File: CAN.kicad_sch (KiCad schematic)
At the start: 5 parts

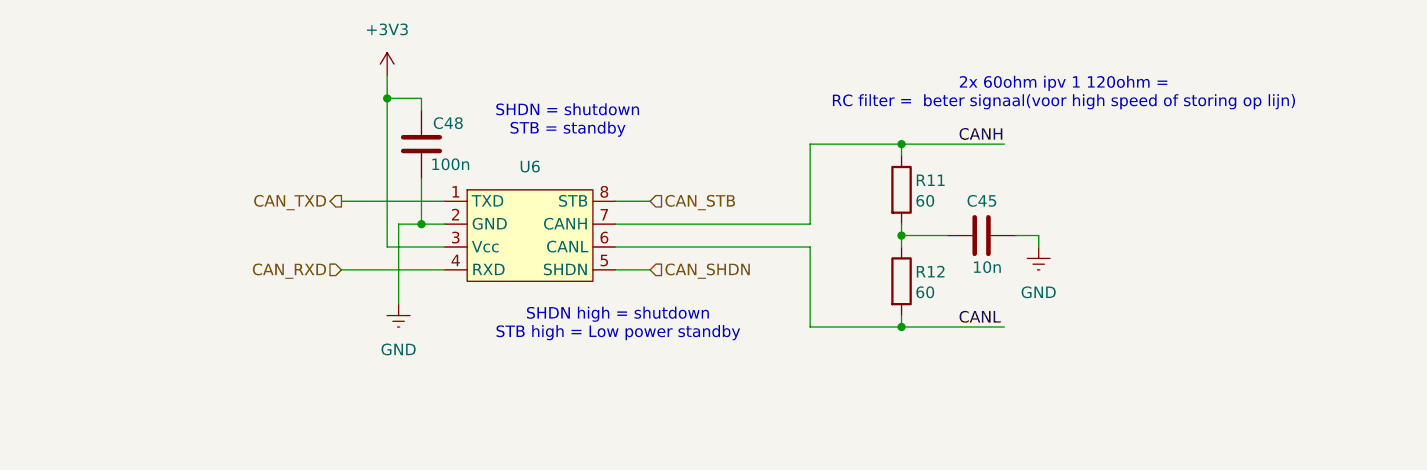
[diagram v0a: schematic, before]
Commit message: footprints
footprints aan de condensators toegevoegd
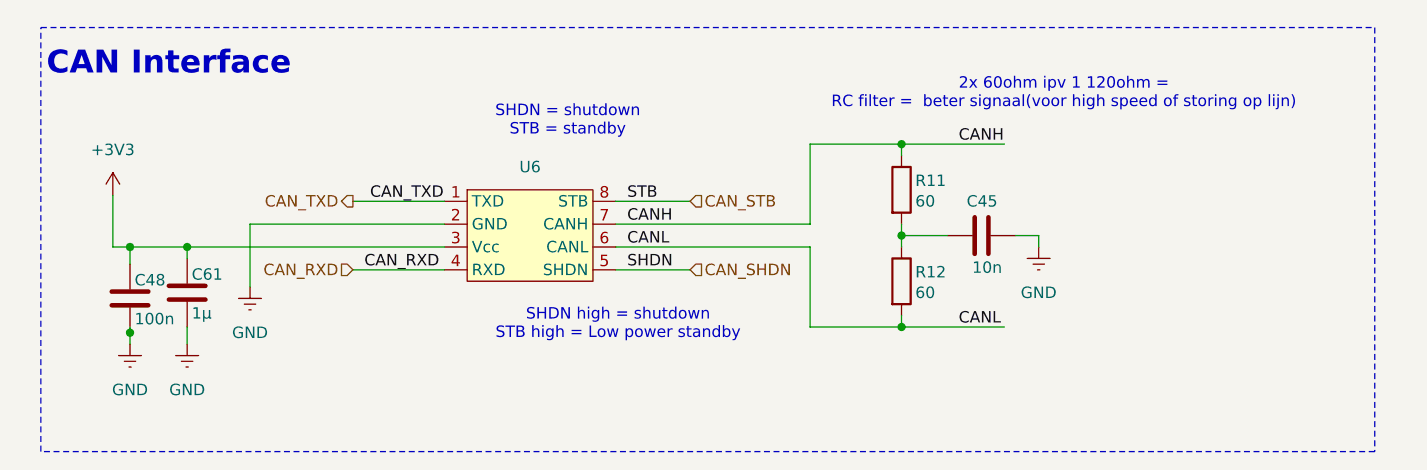
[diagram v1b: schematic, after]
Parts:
- added C61: 1µ, Capacitor_SMD:C_0603_1608Metric, symbol Device:C
- C48: footprint EEPROM:579-24LC32AFT-ISN -> Capacitor_SMD:C_0603_1608Metric
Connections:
- net +3V3: now also C61.1
- net GND: now also C61.2
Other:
- note added: "CAN Interface"

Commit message: schemas klaar
schemas en footprints aan symbolen allemaal juist gemaakt
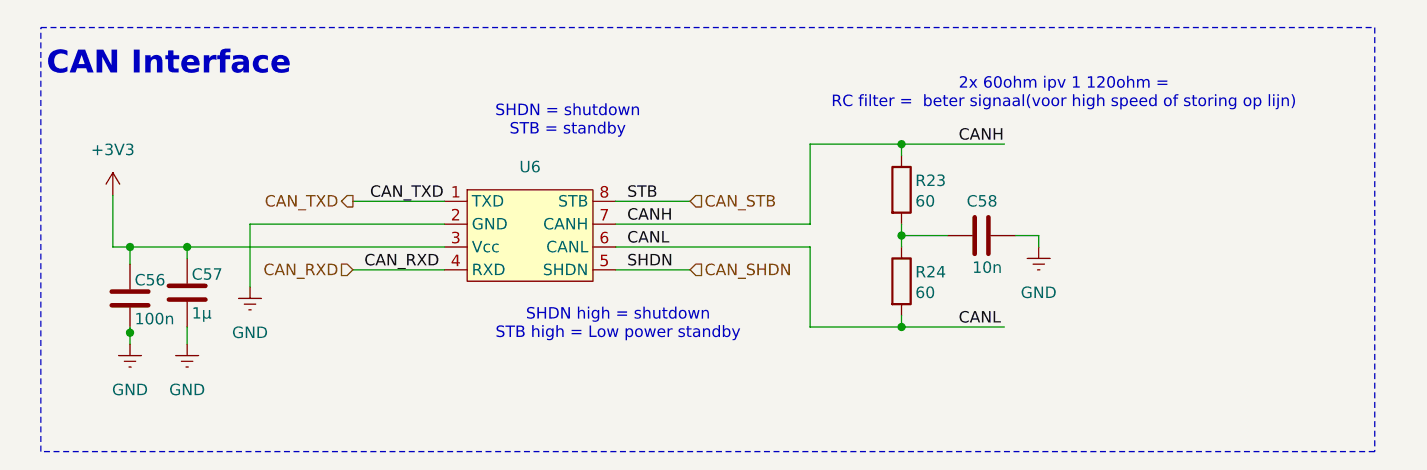
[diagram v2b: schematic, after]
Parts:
- C58: renamed from C45; footprint EEPROM:579-24LC32AFT-ISN -> Capacitor_SMD:C_0603_1608Metric
- R23: renamed from R11; footprint (none) -> Resistor_SMD:R_0603_1608Metric
- R24: renamed from R12; footprint (none) -> Resistor_SMD:R_0603_1608Metric
- renumbered C48 to C56, C61 to C57
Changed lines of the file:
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@@
 		(dnp no)
 		(fields_autoplaced yes)
-		(property "Reference" "#PWR070"
+		(property "Reference" "#PWR069"
 			(at 95.885 97.155 0)
 			(hide yes)
@@
 			(project "ESC_PLC"
 				(path "/5bd3bb6f-fe53-443c-806c-077e2bbb5d14/fe40b710-6ad0-4f5f-80cc-5572b327525f"
-					(reference "#PWR070")
+					(reference "#PWR069")
 					(unit 1)
 				)
@@
 		(in_pos_files yes)
 		(dnp no)
-		(property "Reference" "C61"
+		(property "Reference" "C57"
 			(at 96.393 83.058 0)
 			(show_name no)
@@
 			(project "ESC_PLC"
 				(path "/5bd3bb6f-fe53-443c-806c-077e2bbb5d14/fe40b710-6ad0-4f5f-80cc-5572b327525f"
-					(reference "C61")
+					(reference "C57")
 					(unit 1)
 				)
@@
 		(dnp no)
 		(fields_autoplaced yes)
-		(property "Reference" "#PWR071"
+		(property "Reference" "#PWR068"
 			(at 89.535 97.155 0)
 			(hide yes)
@@
 			(project "ESC_PLC"
 				(path "/5bd3bb6f-fe53-443c-806c-077e2bbb5d14/fe40b710-6ad0-4f5f-80cc-5572b327525f"
-					(reference "#PWR071")
+					(reference "#PWR068")
 					(unit 1)
 				)
@@
 		(dnp no)
 		(fields_autoplaced yes)
-		(property "Reference" "#PWR047"
+		(property "Reference" "#PWR070"
 			(at 102.87 90.805 0)
 			(hide yes)
@@
 			(project "ESC_PLC"
 				(path "/5bd3bb6f-fe53-443c-806c-077e2bbb5d14/fe40b710-6ad0-4f5f-80cc-5572b327525f"
-					(reference "#PWR047")
+					(reference "#PWR070")
 					(unit 1)
 				)
@@
 		(in_pos_files yes)
 		(dnp no)
-		(property "Reference" "R12"
+		(property "Reference" "R24"
 			(at 176.784 82.804 0)
 			(show_name no)
@@
 			)
 		)
-		(property "Footprint" ""
+		(property "Footprint" "Resistor_SMD:R_0603_1608Metric"
 			(at 173.482 83.82 90)
 			(hide yes)
@@
 			(project "ESC_PLC"
 				(path "/5bd3bb6f-fe53-443c-806c-077e2bbb5d14/fe40b710-6ad0-4f5f-80cc-5572b327525f"
-					(reference "R12")
+					(reference "R24")
 					(unit 1)
 				)
@@
 		(dnp no)
 		(fields_autoplaced yes)
-		(property "Reference" "#PWR049"
+		(property "Reference" "#PWR071"
 			(at 190.5 86.36 0)
 			(hide yes)
@@
 			(project "ESC_PLC"
 				(path "/5bd3bb6f-fe53-443c-806c-077e2bbb5d14/fe40b710-6ad0-4f5f-80cc-5572b327525f"
-					(reference "#PWR049")
+					(reference "#PWR071")
 					(unit 1)
 				)
@@
 		(dnp no)
 		(fields_autoplaced yes)
-		(property "Reference" "#PWR048"
+		(property "Reference" "#PWR067"
 			(at 87.63 78.105 0)
 			(hide yes)
@@
 			(project "ESC_PLC"
 				(path "/5bd3bb6f-fe53-443c-806c-077e2bbb5d14/fe40b710-6ad0-4f5f-80cc-5572b327525f"
-					(reference "#PWR048")
+					(reference "#PWR067")
 					(unit 1)
 				)
@@
 		(in_pos_files yes)
 		(dnp no)
-		(property "Reference" "C48"
+		(property "Reference" "C56"
 			(at 90.043 83.693 0)
 			(show_name no)
@@
 			(project "ESC_PLC"
 				(path "/5bd3bb6f-fe53-443c-806c-077e2bbb5d14/fe40b710-6ad0-4f5f-80cc-5572b327525f"
-					(reference "C48")
+					(reference "C56")
 					(unit 1)
 				)
@@
 		(in_pos_files yes)
 		(dnp no)
-		(property "Reference" "C45"
+		(property "Reference" "C58"
 			(at 185.928 74.93 90)
 			(show_name no)
@@
 			)
 		)
-		(property "Footprint" "EEPROM:579-24LC32AFT-ISN"
+		(property "Footprint" "Capacitor_SMD:C_0603_1608Metric"
 			(at 187.96 77.7748 0)
 			(hide yes)
@@
 			(project "ESC_PLC"
 				(path "/5bd3bb6f-fe53-443c-806c-077e2bbb5d14/fe40b710-6ad0-4f5f-80cc-5572b327525f"
-					(reference "C45")
+					(reference "C58")
 					(unit 1)
 				)
@@
 		(in_pos_files yes)
 		(dnp no)
-		(property "Reference" "R11"
+		(property "Reference" "R23"
 			(at 176.784 72.644 0)
 			(show_name no)
@@
 			)
 		)
-		(property "Footprint" ""
+		(property "Footprint" "Resistor_SMD:R_0603_1608Metric"
 			(at 173.482 73.66 90)
 			(hide yes)
@@
 			(project "ESC_PLC"
 				(path "/5bd3bb6f-fe53-443c-806c-077e2bbb5d14/fe40b710-6ad0-4f5f-80cc-5572b327525f"
-					(reference "R11")
-					(unit 1)
-				)
+					(reference "R23")
+					(unit 1)
+				)

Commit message: al de main blokken bij elkaar gezet op juiste plaats
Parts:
- added D5: NUP2105L, Package_TO_SOT_SMD:SOT-23, symbol Power_Protection:NUP2105L
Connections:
- net CANH: now also D5.1 (K)
- net CANL: now also D5.2 (K)
- net GND: now also D5.3 (A)
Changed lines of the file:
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@@
+	)
+	(junction
+		(at 205.74 88.9)
+		(diameter 0)
+		(color 0 0 0 0)
 	)
 	(junction
@@
 	)
 	(junction
+		(at 196.85 68.58)
+		(diameter 0)
+		(color 0 0 0 0)
+	)
+	(junction
 		(at 89.535 89.535)
 		(diameter 0)
@@
 	(wire
 		(pts
+			(xy 199.39 81.28) (xy 199.39 82.55)
+		)
+		(stroke
+			(width 0)
+			(type default)
+		)
+	)
+	(wire
+		(pts
 			(xy 87.63 80.01) (xy 89.535 80.01)
 		)
@@
 	(wire
 		(pts
+			(xy 201.93 69.85) (xy 201.93 71.12)
+		)
+		(stroke
+			(width 0)
+			(type default)
+		)
+	)
+	(wire
+		(pts
 			(xy 89.535 89.535) (xy 89.535 90.805)
 		)
@@
 	(wire
 		(pts
+			(xy 196.85 68.58) (xy 209.55 68.58)
+		)
+		(stroke
+			(width 0)
+			(type default)
+		)
+	)
+	(wire
+		(pts
 			(xy 175.26 78.74) (xy 180.34 78.74)
 		)
@@
 	(wire
 		(pts
+			(xy 205.74 69.85) (xy 205.74 88.9)
+		)
+		(stroke
+			(width 0)
+			(type default)
+		)
+	)
+	(wire
+		(pts
+			(xy 205.74 88.9) (xy 209.55 88.9)
+		)
+		(stroke
+			(width 0)
+			(type default)
+		)
+	)
+	(wire
+		(pts
+			(xy 196.85 68.58) (xy 196.85 71.12)
+		)
+		(stroke
+			(width 0)
+			(type default)
+		)
+	)
+	(wire
+		(pts
+			(xy 201.93 69.85) (xy 205.74 69.85)
+		)
+		(stroke
+			(width 0)
+			(type default)
+		)
+	)
+	(wire
+		(pts
 			(xy 95.885 88.9) (xy 95.885 90.805)
 		)
@@
 	(wire
 		(pts
-			(xy 175.26 68.58) (xy 186.69 68.58)
+			(xy 175.26 68.58) (xy 196.85 68.58)
 		)
 		(stroke
@@
 	(wire
 		(pts
-			(xy 175.26 88.9) (xy 186.69 88.9)
+			(xy 175.26 88.9) (xy 205.74 88.9)
 		)
 		(stroke
@@
 	)
 	(label "CANH"
-		(at 181.61 68.58 0)
+		(at 209.55 68.58 0)
 		(effects
 			(font
@@
 	)
 	(label "CANL"
-		(at 181.61 88.9 0)
+		(at 209.55 88.9 0)
 		(effects
 			(font
@@
 	)
 	(symbol
+		(lib_id "Power_Protection:NUP2105L")
+		(at 199.39 76.2 0)
+		(unit 1)
+		(body_style 1)
+		(exclude_from_sim no)
+		(in_bom yes)
+		(on_board yes)
+		(in_pos_files yes)
+		(dnp no)
+		(property "Reference" "D5"
+			(at 206.502 74.168 0)
+			(show_name no)
+			(do_not_autoplace no)
+			(effects
+				(font
+					(size 1.27 1.27)
+				)
+				(justify left)
+			)
+		)
+		(property "Value" "NUP2105L"
+			(at 206.756 76.454 0)
+			(show_name no)
+			(do_not_autoplace no)
+			(effects
+				(font
+					(size 1.27 1.27)
+				)
+				(justify left)
+			)
+		)
+		(property "Footprint" "Package_TO_SOT_SMD:SOT-23"
+			(at 205.105 77.47 0)
+			(hide yes)
+			(show_name no)
+			(do_not_autoplace no)
+			(effects
+				(font
+					(size 1.27 1.27)
+				)
+				(justify left)
+			)
+		)
+		(property "Datasheet" "https://www.onsemi.com/pub_link/Collateral/NUP2105L-D.PDF"
+			(at 202.565 73.025 0)
+			(hide yes)
+			(show_name no)
+			(do_not_autoplace no)
+			(effects
+				(font
+					(size 1.27 1.27)
+				)
+			)
+		)
+		(property "Description" "Dual Line CAN Bus Protector, 24Vrwm"
+			(at 199.39 76.2 0)
+			(hide yes)
+			(show_name no)
+			(do_not_autoplace no)
+			(effects
+				(font
+					(size 1.27 1.27)
+				)
+			)
+		)
+		(pin "1"
+		)
+		(pin "3"
+		)
+		(pin "2"
+		)
+		(instances
+			(project "ESC_PLC"
+				(path "/5bd3bb6f-fe53-443c-806c-077e2bbb5d14/fe40b710-6ad0-4f5f-80cc-5572b327525f"
+					(reference "D5")
+					(unit 1)
+				)
+			)
+		)
+	)
+	(symbol
 		(lib_id "power:GNDREF")
 		(at 102.87 84.455 0)
@@
 		(in_pos_files yes)
 		(dnp no)
-		(fields_autoplaced yes)
 		(property "Reference" "#PWR071"
 			(at 190.5 86.36 0)
@@
 		)
 		(property "Value" "GND"
-			(at 190.5 85.09 0)
+			(at 190.5 84.328 0)
 			(show_name no)
 			(do_not_autoplace no)
@@
 					(unit 1)
 				)
+			)
+		)
+	)
+	(symbol
+		(lib_id "power:GNDREF")
+		(at 199.39 82.55 0)
+		(unit 1)
+		(body_style 1)
+		(exclude_from_sim no)
+		(in_bom yes)
+		(on_board yes)
+		(in_pos_files yes)
+		(dnp no)
+		(property "Reference" "#PWR0105"
+			(at 199.39 88.9 0)
+			(hide yes)
+			(show_name no)
+			(do_not_autoplace no)
+			(effects
+				(font
+					(size 1.27 1.27)
+				)
+			)
+		)
+		(property "Value" "GND"
+			(at 199.39 86.614 0)
+			(show_name no)
+			(do_not_autoplace no)
+			(effects
+				(font
+					(size 1.27 1.27)
+				)
+			)
+		)
+		(property "Footprint" ""
+			(at 199.39 82.55 0)
+			(hide yes)
+			(show_name no)
+			(do_not_autoplace no)
+			(effects
+				(font
+					(size 1.27 1.27)
+				)
+			)
+		)
+		(property "Datasheet" ""
+			(at 199.39 82.55 0)
+			(hide yes)
+			(show_name no)
+			(do_not_autoplace no)
+			(effects
+				(font
+					(size 1.27 1.27)
+				)
+			)
+		)
+		(property "Description" "Power symbol creates a global label with name \"GNDREF\" , reference supply ground"
+			(at 199.39 82.55 0)
+			(hide yes)
+			(show_name no)
+			(do_not_autoplace no)
+			(effects
+				(font
+					(size 1.27 1.27)
+				)
+			)
+		)
+		(pin "1"
+		)
+		(instances
+			(project "ESC_PLC"
+				(path "/5bd3bb6f-fe53-443c-806c-077e2bbb5d14/fe40b710-6ad0-4f5f-80cc-5572b327525f"
+					(reference "#PWR0105")
+					(unit 1)
+				)

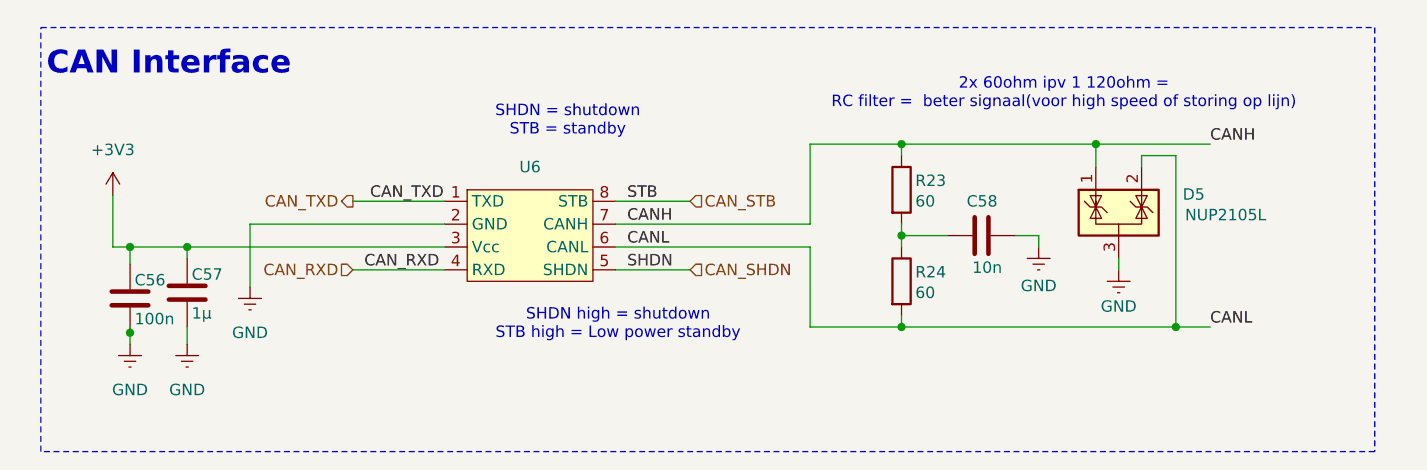
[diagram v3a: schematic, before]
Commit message: connector
connector toegevoegd en wat pinnen aangepast
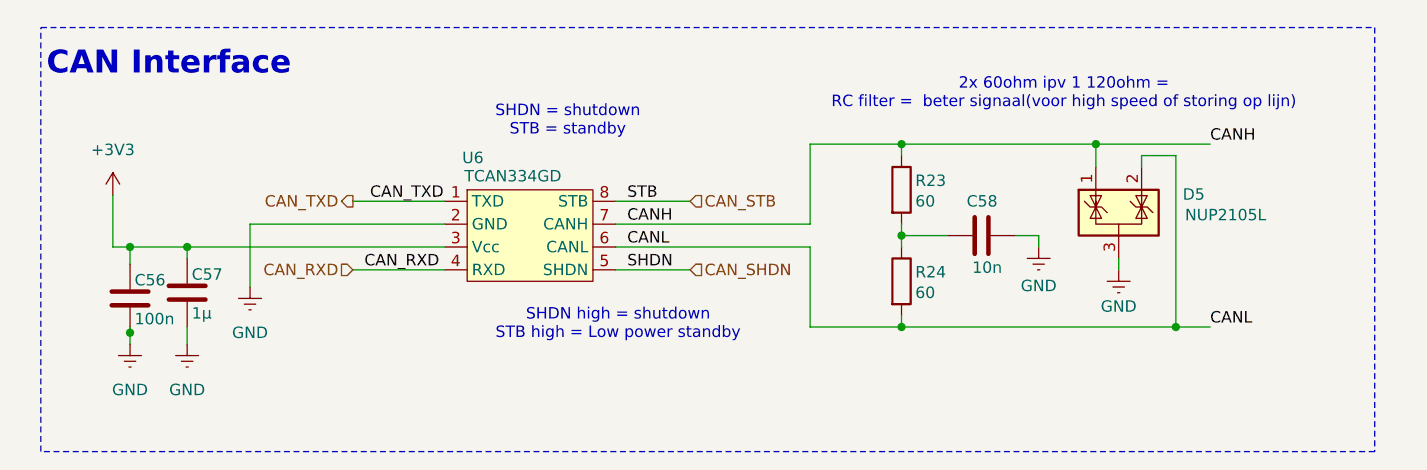
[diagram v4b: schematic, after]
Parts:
- U6: value (none) -> TCAN334GD
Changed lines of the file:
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@@
 		(in_pos_files yes)
 		(dnp no)
-		(fields_autoplaced yes)
 		(property "Reference" "U6"
-			(at 133.985 71.12 0)
+			(at 127.635 70.104 0)
 			(show_name no)
 			(do_not_autoplace no)
@@
 			)
 		)
-		(property "Value" ""
-			(at 127 73.66 0)
+		(property "Value" "TCAN334GD"
+			(at 132.08 72.136 0)
 			(show_name no)
 			(do_not_autoplace no)

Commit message: schema's finalized
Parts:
- added J5: Screw_Terminal_01x02, symbol Connector:Screw_Terminal_01x02
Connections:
- net CANH: now also J5.1 (Pin_1)
- net CANL: now also J5.2 (Pin_2)
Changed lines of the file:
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@@
 	(rectangle
 		(start 79.629 55.626)
-		(end 227.838 102.743)
+		(end 231.648 102.743)
 		(stroke
 			(width 0)
@@
 	(wire
 		(pts
+			(xy 217.17 79.375) (xy 217.17 88.9)
+		)
+		(stroke
+			(width 0)
+			(type default)
+		)
+	)
+	(wire
+		(pts
 			(xy 89.535 80.01) (xy 89.535 81.915)
 		)
@@
 	(wire
 		(pts
+			(xy 219.075 76.835) (xy 217.17 76.835)
+		)
+		(stroke
+			(width 0)
+			(type default)
+		)
+	)
+	(wire
+		(pts
 			(xy 114.3 82.55) (xy 124.46 82.55)
 		)
@@
 	(wire
 		(pts
+			(xy 217.17 76.835) (xy 217.17 68.58)
+		)
+		(stroke
+			(width 0)
+			(type default)
+		)
+	)
+	(wire
+		(pts
 			(xy 175.26 78.74) (xy 175.26 80.01)
 		)
@@
 	(wire
 		(pts
-			(xy 196.85 68.58) (xy 209.55 68.58)
+			(xy 196.85 68.58) (xy 217.17 68.58)
 		)
 		(stroke
@@
 	(wire
 		(pts
-			(xy 205.74 88.9) (xy 209.55 88.9)
+			(xy 205.74 88.9) (xy 217.17 88.9)
 		)
 		(stroke
@@
 		(pts
 			(xy 175.26 77.47) (xy 175.26 78.74)
+		)
+		(stroke
+			(width 0)
+			(type default)
+		)
+	)
+	(wire
+		(pts
+			(xy 219.075 79.375) (xy 217.17 79.375)
 		)
 		(stroke
@@
 					(unit 1)
 				)
+			)
+		)
+	)
+	(symbol
+		(lib_id "Connector:Screw_Terminal_01x02")
+		(at 224.155 76.835 0)
+		(unit 1)
+		(body_style 1)
+		(exclude_from_sim no)
+		(in_bom yes)
+		(on_board yes)
+		(in_pos_files yes)
+		(dnp no)
+		(fields_autoplaced yes)
+		(property "Reference" "J5"
+			(at 227.33 76.8349 0)
+			(show_name no)
+			(do_not_autoplace no)
+			(effects
+				(font
+					(size 1.27 1.27)
+				)
+				(justify left)
+			)
+		)
+		(property "Value" "Screw_Terminal_01x02"
+			(at 227.33 79.3749 0)
+			(hide yes)
+			(show_name no)
+			(do_not_autoplace no)
+			(effects
+				(font
+					(size 1.27 1.27)
+				)
+				(justify left)
+			)
+		)
+		(property "Footprint" ""
+			(at 224.155 76.835 0)
+			(hide yes)
+			(show_name no)
+			(do_not_autoplace no)
+			(effects
+				(font
+					(size 1.27 1.27)
+				)
+			)
+		)
+		(property "Datasheet" ""
+			(at 224.155 76.835 0)
+			(hide yes)
+			(show_name no)
+			(do_not_autoplace no)
+			(effects
+				(font
+					(size 1.27 1.27)
+				)
+			)
+		)
+		(property "Description" "Generic screw terminal, single row, 01x02, script generated (kicad-library-utils/schlib/autogen/connector/)"
+			(at 224.155 76.835 0)
+			(hide yes)
+			(show_name no)
+			(do_not_autoplace no)
+			(effects
+				(font
+					(size 1.27 1.27)
+				)
+			)
+		)
+		(pin "1"
+		)
+		(pin "2"
+		)
+		(instances
+			(project "ESC_PLC"
+				(path "/5bd3bb6f-fe53-443c-806c-077e2bbb5d14/fe40b710-6ad0-4f5f-80cc-5572b327525f"
+					(reference "J5")
+					(unit 1)
+				)
